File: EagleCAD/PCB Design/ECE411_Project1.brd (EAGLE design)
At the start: 160 x 100 mm, 29 parts, among them J1 0473460001_USBMICRO, SW1 FSM2JSMLTR, U1 ATS160SM-1, U2 MIC29310-5.0WU, U3 NCP5501DT50RKG

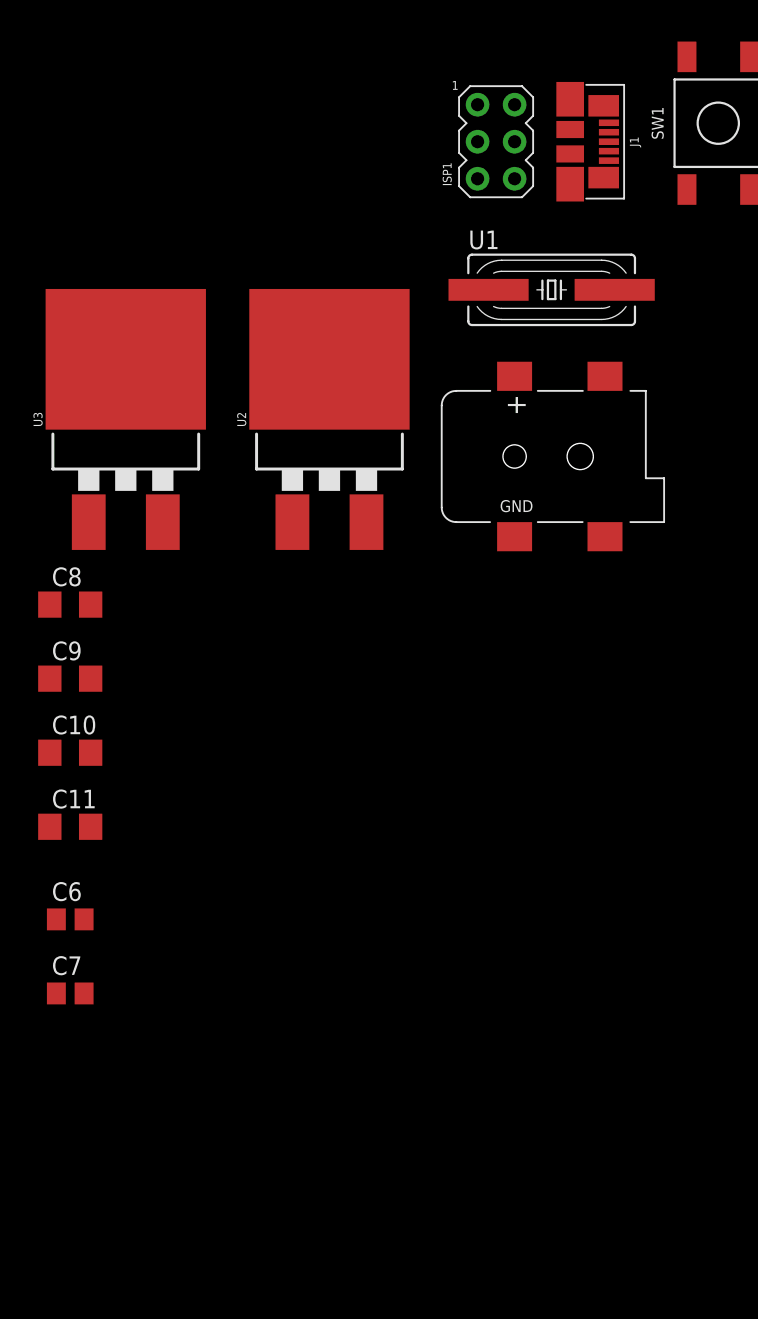
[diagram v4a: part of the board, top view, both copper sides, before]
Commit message: Updated schematic with new DC barrel component that is thru-hole 2.1MM size
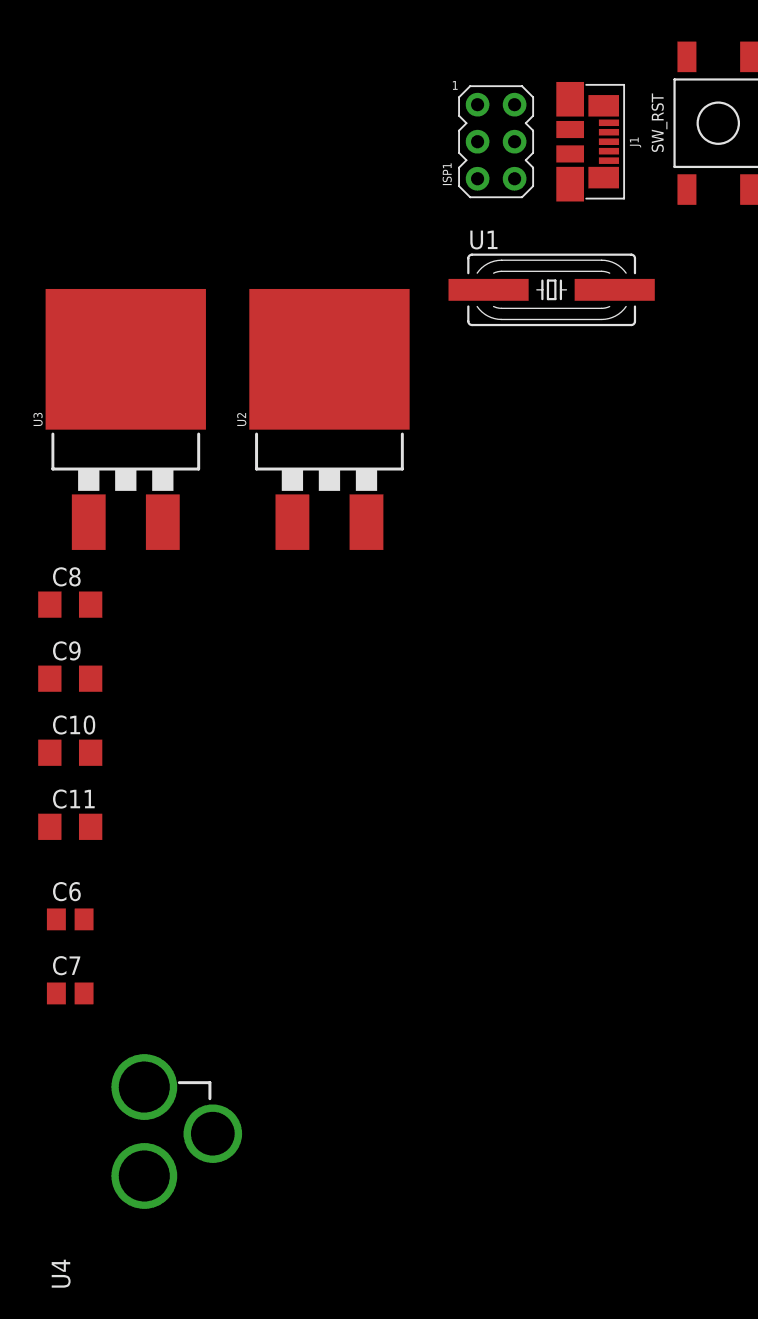
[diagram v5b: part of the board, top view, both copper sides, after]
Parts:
- removed CN1: (no value), adafruit:DCJACK_2MM_SMT
- added U4: DCJACK_2.1MM_PTH, DCBARREL_2.1MM:DCJACK_2.1MM_PTH
- renumbered SW1 to SW_RST
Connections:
- net N$1 renamed D+USB
- net N$2 renamed D+MCU
- net N$3 renamed D-USB
- net N$4 renamed D-MCU
- net GND: now also U4.GND, U4.GNDBREAK; no longer CN1.GND, CN1.GNDBREAK
- net N$22: now also U4.PWR; no longer CN1.PWR1
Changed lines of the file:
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@@
 <element name="LED2" library="led" library_urn="urn:adsk.eagle:library:259" package="1206" package3d_urn="urn:adsk.eagle:package:15796/1" value="" x="-67.31" y="-15.24"/>
 <element name="LED1" library="led" library_urn="urn:adsk.eagle:library:259" package="1206" package3d_urn="urn:adsk.eagle:package:15796/1" value="" x="-67.31" y="-20.32"/>
-<element name="SW1" library="Push_Button" package="FSM2JSMLTR" value="FSM2JSMLTR" x="-73.66" y="-49.53"/>
+<element name="SW_RST" library="Push_Button" package="FSM2JSMLTR" value="FSM2JSMLTR" x="-73.66" y="-49.53"/>
 <element name="J1" library="USB_Micro_and_AVRISP" package="MOLEX_USBMICRO" value="0473460001_USBMICRO" x="-83.82" y="-50.8"/>
 <element name="ISP1" library="USB_Micro_and_AVRISP" package="AVRISP" value="AVRISP-6" x="-88.9" y="-50.8"/>
 <element name="U1" library="Xtals" package="ATS160SM-1" value="ATS160SM-1" x="-85.09" y="-60.96"/>
-<element name="CN1" library="adafruit" library_urn="urn:adsk.eagle:library:420" package="DCJACK_2MM_SMT" package3d_urn="urn:adsk.eagle:package:6240730/1" value="" x="-87.63" y="-72.39"/>
 <element name="U2" library="Regulators" package="TO-263/D2PAK" value="MIC29310-5.0WU" x="-100.33" y="-69.85"/>
 <element name="U3" library="Regulators" package="TO-263/D2PAK" value="NCP5501DT50RKG" x="-114.3" y="-69.85"/>
@@
 <attribute name="SPICEPREFIX" value="C" x="-118.11" y="-109.22" size="1.778" layer="27" display="off"/>
 </element>
+<element name="U4" library="DCBARREL_2.1MM" package="DCJACK_2.1MM_PTH" value="DCJACK_2.1MM_PTH" x="-113.03" y="-129.54"/>
 </elements>
 <signals>
@@
 <contactref element="C4" pad="1"/>
 <contactref element="C3" pad="1"/>
-<contactref element="SW1" pad="4"/>
-<contactref element="SW1" pad="2"/>
+<contactref element="SW_RST" pad="4"/>
+<contactref element="SW_RST" pad="2"/>
 <contactref element="J1" pad="5"/>
 <contactref element="J1" pad="G6"/>
@@
 <contactref element="U2" pad="2"/>
 <contactref element="U3" pad="2"/>
-<contactref element="CN1" pad="GND"/>
-<contactref element="CN1" pad="GNDBREAK"/>
 <contactref element="C8" pad="2"/>
 <contactref element="C11" pad="2"/>
@@
 <contactref element="C6" pad="1"/>
 <contactref element="C7" pad="1"/>
+<contactref element="U4" pad="GND"/>
+<contactref element="U4" pad="GNDBREAK"/>
+<wire x1="-108.33" y1="-118.84" x2="-113.03" y2="-121.74" width="0" layer="19" extent="1-1"/>
+<wire x1="-119.06" y1="-109.22" x2="-113.03" y2="-121.74" width="0" layer="19" extent="1-1"/>
 <wire x1="-119.06" y1="-104.14" x2="-119.06" y2="-109.22" width="0" layer="19" extent="1-1"/>
 <wire x1="-116.71" y1="-97.79" x2="-119.06" y2="-104.14" width="0" layer="19" extent="1-1"/>
@@
 <wire x1="-114.3" y1="-65.725" x2="-116.71" y2="-82.55" width="0" layer="19" extent="1-1"/>
 <wire x1="-100.33" y1="-65.725" x2="-114.3" y2="-65.725" width="0" layer="19" extent="1-1"/>
-<wire x1="-87.63" y1="-77.89" x2="-100.33" y2="-65.725" width="0" layer="19" extent="1-1"/>
-<wire x1="-81.43" y1="-77.89" x2="-87.63" y2="-77.89" width="0" layer="19" extent="1-1"/>
 <wire x1="-87.63" y1="-53.34" x2="-100.33" y2="-65.725" width="0" layer="19" extent="1-1"/>
 <wire x1="-83.82" y1="-53.7125" x2="-87.63" y2="-53.34" width="0" layer="19" extent="1-1"/>
@@
 <wire x1="-15.24" y1="73.66" x2="-17.91" y2="68.58" width="0" layer="19" extent="1-1"/>
 </signal>
-<signal name="N$1">
+<signal name="D+USB">
 <contactref element="R1" pad="1"/>
 <contactref element="J1" pad="3"/>
 <wire x1="-28.092" y1="68.58" x2="-81.16" y2="-50.8" width="0" layer="19" extent="1-1"/>
 </signal>
-<signal name="N$2">
+<signal name="D+MCU">
 <contactref element="U$1" pad="4"/>
 <contactref element="R1" pad="2"/>
 <wire x1="-59.14" y1="35.89" x2="-25.248" y2="68.58" width="0" layer="19" extent="1-1"/>
 </signal>
-<signal name="N$3">
+<signal name="D-USB">
 <contactref element="R2" pad="1"/>
 <contactref element="J1" pad="2"/>
 <wire x1="-33.172" y1="68.58" x2="-81.16" y2="-50.15" width="0" layer="19" extent="1-1"/>
 </signal>
-<signal name="N$4">
+<signal name="D-MCU">
 <contactref element="U$1" pad="3"/>
 <contactref element="R2" pad="2"/>
@@
 <contactref element="U$1" pad="13"/>
 <contactref element="R5" pad="1"/>
-<contactref element="SW1" pad="3"/>
-<contactref element="SW1" pad="1"/>
+<contactref element="SW_RST" pad="3"/>
+<contactref element="SW_RST" pad="1"/>
 <contactref element="ISP1" pad="5"/>
 <wire x1="-75.81" y1="-44.98" x2="-90.17" y2="-53.34" width="0" layer="19" extent="1-1"/>
@@
 </signal>
 <signal name="N$22">
-<contactref element="CN1" pad="PWR1"/>
 <contactref element="U3" pad="1"/>
 <contactref element="U2" pad="1"/>
 <contactref element="C8" pad="1"/>
 <contactref element="C9" pad="1"/>
+<contactref element="U4" pad="PWR"/>
+<wire x1="-119.51" y1="-87.63" x2="-113.03" y2="-115.64" width="0" layer="19" extent="1-1"/>
 <wire x1="-119.51" y1="-82.55" x2="-119.51" y2="-87.63" width="0" layer="19" extent="1-1"/>
 <wire x1="-116.84" y1="-76.895" x2="-119.51" y2="-82.55" width="0" layer="19" extent="1-1"/>
 <wire x1="-102.87" y1="-76.895" x2="-116.84" y2="-76.895" width="0" layer="19" extent="1-1"/>
-<wire x1="-87.63" y1="-66.89" x2="-102.87" y2="-76.895" width="0" layer="19" extent="1-1"/>
 </signal>
 </signals>

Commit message: Started the PCB - Everything's on the board and messy!
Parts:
- moved U4 293.6 mm to (148.6, 3.81)
- moved C11 268.4 mm to (131.1, 1.79), turned to 180 degrees
- moved C10 257.7 mm to (121.4, 2.29)
- moved U2 243.5 mm to (128.3, 14.0)
- moved C9 242.6 mm to (107.4, 1.87)
- moved U3 233.5 mm to (104.1, 12.7)
- moved C8 228.5 mm to (94.0, 2.61), turned to 270 degrees
- moved SERVO1 218.6 mm to (153.7, 73.7), turned to 90 degrees
- moved BUTTON_PAD 208.4 mm to (153.7, 90.2), turned to 90 degrees
- moved C6 206.5 mm to (51.4, 13.9)
- moved C7 203.8 mm to (44.4, 13.8)
- moved SERVO2 171.8 mm to (153.7, 62.2), turned to 90 degrees
- moved J1 164.5 mm to (5.08, 87.6)
- moved U1 148.8 mm to (47.0, 7.62)
- moved ISP1 120.2 mm to (5.08, 24.1)
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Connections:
- net N$20 renamed XTAL2
- net N$21 renamed XTAL1
- net N$22 renamed UNREG_PWR
- net N$5 renamed UCAP
- removed net N$15: ISP1.2
- new net GNDBREAK: U4.GNDBREAK
- net GND: no longer U4.GNDBREAK
- net VCC: now also ISP1.2

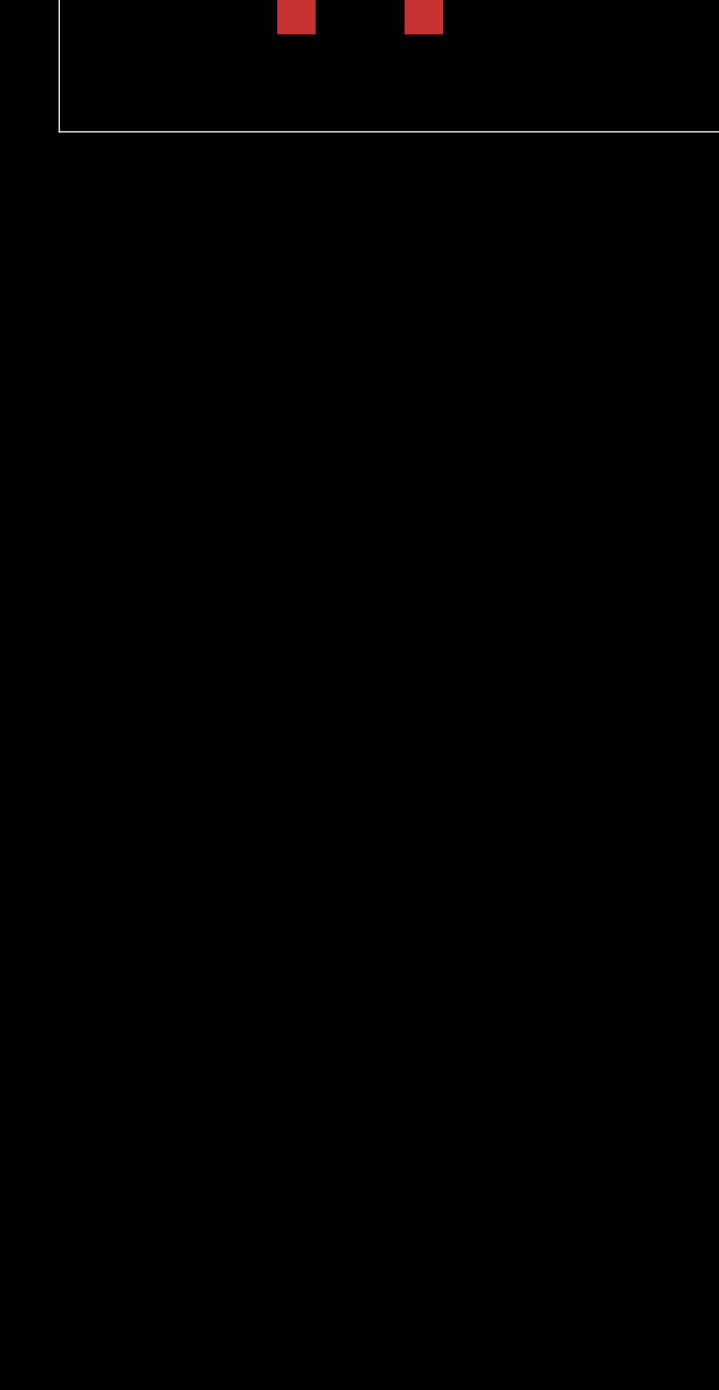
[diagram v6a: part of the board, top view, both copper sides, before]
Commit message: Added test points all over the place
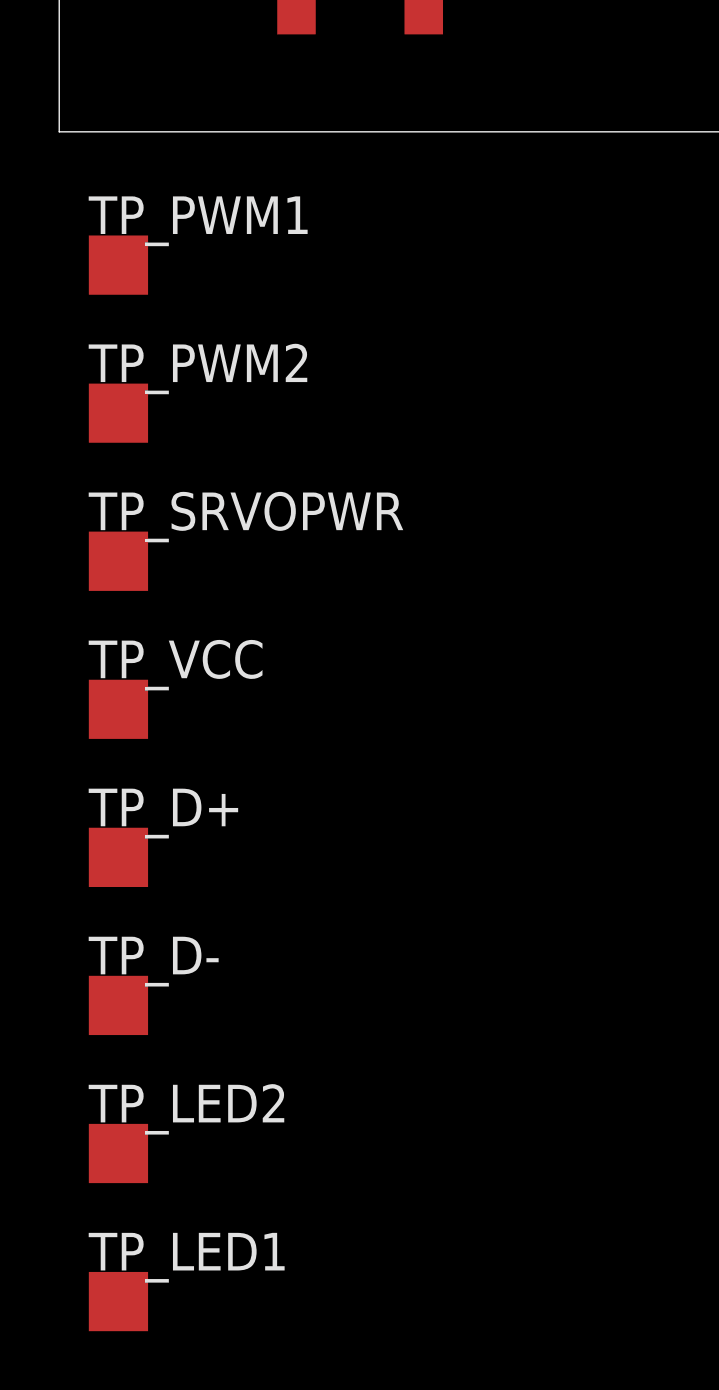
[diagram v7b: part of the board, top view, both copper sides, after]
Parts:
- added TP_D+, TP_D-, TP_LED1, TP_LED2, TP_PWM1, TP_PWM2, TP_SRVOPWR, TP_VCC: TPTP20SQ, BeagleBone_Blue_R3:TP20SQ
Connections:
- net D+MCU: now also TP_D+.TP
- net D-MCU: now also TP_D-.TP
- net N$6: now also TP_LED2.TP
- net N$8: now also TP_LED1.TP
- net PWM1: now also TP_PWM1.TP
- net PWM2: now also TP_PWM2.TP
- net SERVO_PWR: now also TP_SRVOPWR.TP
- net VCC: now also TP_VCC.TP
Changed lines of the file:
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@@
 </element>
 <element name="U4" library="DCBARREL_2.1MM" package="DCJACK_2.1MM_PTH" value="DCJACK_2.1MM_PTH" x="148.59" y="3.81"/>
+<element name="TP_PWM1" library="BeagleBone_Blue_R3" library_urn="urn:adsk.eagle:library:5828899" package="TP20SQ" package3d_urn="urn:adsk.eagle:package:5829471/1" value="TPTP20SQ" x="2" y="-4.5">
+<attribute name="TP_SIGNAL_NAME" value="" x="2" y="-4.5" size="1.778" layer="27" display="off"/>
+</element>
+<element name="TP_PWM2" library="BeagleBone_Blue_R3" library_urn="urn:adsk.eagle:library:5828899" package="TP20SQ" package3d_urn="urn:adsk.eagle:package:5829471/1" value="TPTP20SQ" x="2" y="-9.5">
+<attribute name="TP_SIGNAL_NAME" value="" x="2" y="-9.5" size="1.778" layer="27" display="off"/>
+</element>
+<element name="TP_SRVOPWR" library="BeagleBone_Blue_R3" library_urn="urn:adsk.eagle:library:5828899" package="TP20SQ" package3d_urn="urn:adsk.eagle:package:5829471/1" value="TPTP20SQ" x="2" y="-14.5">
+<attribute name="TP_SIGNAL_NAME" value="" x="2" y="-14.5" size="1.778" layer="27" display="off"/>
+</element>
+<element name="TP_VCC" library="BeagleBone_Blue_R3" library_urn="urn:adsk.eagle:library:5828899" package="TP20SQ" package3d_urn="urn:adsk.eagle:package:5829471/1" value="TPTP20SQ" x="2" y="-19.5">
+<attribute name="TP_SIGNAL_NAME" value="" x="2" y="-19.5" size="1.778" layer="27" display="off"/>
+</element>
+<element name="TP_D+" library="BeagleBone_Blue_R3" library_urn="urn:adsk.eagle:library:5828899" package="TP20SQ" package3d_urn="urn:adsk.eagle:package:5829471/1" value="TPTP20SQ" x="2" y="-24.5">
+<attribute name="TP_SIGNAL_NAME" value="" x="2" y="-24.5" size="1.778" layer="27" display="off"/>
+</element>
+<element name="TP_D-" library="BeagleBone_Blue_R3" library_urn="urn:adsk.eagle:library:5828899" package="TP20SQ" package3d_urn="urn:adsk.eagle:package:5829471/1" value="TPTP20SQ" x="2" y="-29.5">
+<attribute name="TP_SIGNAL_NAME" value="" x="2" y="-29.5" size="1.778" layer="27" display="off"/>
+</element>
+<element name="TP_LED2" library="BeagleBone_Blue_R3" library_urn="urn:adsk.eagle:library:5828899" package="TP20SQ" package3d_urn="urn:adsk.eagle:package:5829471/1" value="TPTP20SQ" x="2" y="-34.5">
+<attribute name="TP_SIGNAL_NAME" value="" x="2" y="-34.5" size="1.778" layer="27" display="off"/>
+</element>
+<element name="TP_LED1" library="BeagleBone_Blue_R3" library_urn="urn:adsk.eagle:library:5828899" package="TP20SQ" package3d_urn="urn:adsk.eagle:package:5829471/1" value="TPTP20SQ" x="2" y="-39.5">
+<attribute name="TP_SIGNAL_NAME" value="" x="2" y="-39.5" size="1.778" layer="27" display="off"/>
+</element>
 </elements>
 <signals>
@@
 <contactref element="U$1" pad="4"/>
 <contactref element="R1" pad="2"/>
+<contactref element="TP_D+" pad="TP"/>
 <wire x1="14.52" y1="25.73" x2="40.252" y2="73.58" width="0" layer="19" extent="1-1"/>
+<wire x1="2" y1="-24.5" x2="14.52" y2="25.73" width="0" layer="19" extent="1-1"/>
 </signal>
 <signal name="D-USB">
@@
 <contactref element="U$1" pad="3"/>
 <contactref element="R2" pad="2"/>
+<contactref element="TP_D-" pad="TP"/>
 <wire x1="14.52" y1="26.53" x2="35.172" y2="73.58" width="0" layer="19" extent="1-1"/>
+<wire x1="2" y1="-29.5" x2="14.52" y2="26.53" width="0" layer="19" extent="1-1"/>
 </signal>
 <signal name="UCAP">
@@
 <contactref element="U$1" pad="18"/>
 <contactref element="R3" pad="2"/>
+<contactref element="TP_LED2" pad="TP"/>
 <wire x1="21.12" y1="18.33" x2="12.112" y2="55.69" width="0" layer="19" extent="1-1"/>
+<wire x1="2" y1="-34.5" x2="21.12" y2="18.33" width="0" layer="19" extent="1-1"/>
 </signal>
 <signal name="N$9">
@@
 <contactref element="C10" pad="1"/>
 <contactref element="ISP1" pad="2"/>
+<contactref element="TP_VCC" pad="TP"/>
 <wire x1="106.68" y1="5.655" x2="119.99" y2="2.29" width="0" layer="19" extent="1-1"/>
-<wire x1="6.35" y1="26.67" x2="106.68" y2="5.655" width="0" layer="19" extent="1-1"/>
-<wire x1="17.92" y1="18.33" x2="6.35" y2="26.67" width="0" layer="19" extent="1-1"/>
-<wire x1="26.12" y1="20.93" x2="17.92" y2="18.33" width="0" layer="19" extent="1-1"/>
-<wire x1="24.32" y1="29.93" x2="26.12" y2="20.93" width="0" layer="19" extent="1-1"/>
+<wire x1="40.39" y1="39.58" x2="106.68" y2="5.655" width="0" layer="19" extent="1-1"/>
+<wire x1="34.79" y1="39.53" x2="40.39" y2="39.58" width="0" layer="19" extent="1-1"/>
+<wire x1="28.44" y1="39.53" x2="34.79" y2="39.53" width="0" layer="19" extent="1-1"/>
+<wire x1="22.09" y1="39.53" x2="28.44" y2="39.53" width="0" layer="19" extent="1-1"/>
+<wire x1="24.32" y1="29.93" x2="22.09" y2="39.53" width="0" layer="19" extent="1-1"/>
 <wire x1="16.32" y1="29.93" x2="24.32" y2="29.93" width="0" layer="19" extent="1-1"/>
-<wire x1="28.44" y1="39.53" x2="16.32" y2="29.93" width="0" layer="19" extent="1-1"/>
-<wire x1="22.09" y1="39.53" x2="28.44" y2="39.53" width="0" layer="19" extent="1-1"/>
-<wire x1="34.79" y1="39.53" x2="28.44" y2="39.53" width="0" layer="19" extent="1-1"/>
-<wire x1="30.092" y1="73.58" x2="34.79" y2="39.53" width="0" layer="19" extent="1-1"/>
-<wire x1="40.39" y1="39.58" x2="30.092" y2="73.58" width="0" layer="19" extent="1-1"/>
+<wire x1="26.12" y1="20.93" x2="24.32" y2="29.93" width="0" layer="19" extent="1-1"/>
+<wire x1="17.92" y1="18.33" x2="26.12" y2="20.93" width="0" layer="19" extent="1-1"/>
+<wire x1="6.35" y1="26.67" x2="16.32" y2="29.93" width="0" layer="19" extent="1-1"/>
+<wire x1="30.092" y1="73.58" x2="28.44" y2="39.53" width="0" layer="19" extent="1-1"/>
+<wire x1="2" y1="-19.5" x2="17.92" y2="18.33" width="0" layer="19" extent="1-1"/>
 </signal>
 <signal name="PWM2">
 <contactref element="U$1" pad="29"/>
 <contactref element="SERVO2" pad="1"/>
+<contactref element="TP_PWM2" pad="TP"/>
 <wire x1="26.12" y1="24.93" x2="153.67" y2="59.69" width="0" layer="19" extent="1-1"/>
+<wire x1="2" y1="-9.5" x2="26.12" y2="24.93" width="0" layer="19" extent="1-1"/>
 </signal>
 <signal name="PWM1">
 <contactref element="U$1" pad="30"/>
 <contactref element="SERVO1" pad="1"/>
-<wire x1="153.67" y1="71.12" x2="26.12" y2="25.73" width="0" layer="19" extent="1-1"/>
+<contactref element="TP_PWM1" pad="TP"/>
+<wire x1="26.12" y1="25.73" x2="153.67" y2="71.12" width="0" layer="19" extent="1-1"/>
+<wire x1="2" y1="-4.5" x2="26.12" y2="25.73" width="0" layer="19" extent="1-1"/>
 </signal>
 <signal name="N$8">
 <contactref element="U$1" pad="19"/>
 <contactref element="R4" pad="2"/>
+<contactref element="TP_LED1" pad="TP"/>
 <wire x1="21.92" y1="18.33" x2="12.112" y2="50.61" width="0" layer="19" extent="1-1"/>
+<wire x1="2" y1="-39.5" x2="21.92" y2="18.33" width="0" layer="19" extent="1-1"/>
 </signal>
 <signal name="N$7">
@@
 <contactref element="U2" pad="3"/>
 <contactref element="C11" pad="1"/>
-<wire x1="130.81" y1="6.925" x2="132.51" y2="1.79" width="0" layer="19" extent="1-1"/>
-<wire x1="153.67" y1="73.66" x2="130.81" y2="6.925" width="0" layer="19" extent="1-1"/>
+<contactref element="TP_SRVOPWR" pad="TP"/>
 <wire x1="153.67" y1="62.23" x2="153.67" y2="73.66" width="0" layer="19" extent="1-1"/>
+<wire x1="130.81" y1="6.925" x2="153.67" y2="62.23" width="0" layer="19" extent="1-1"/>
+<wire x1="132.51" y1="1.79" x2="130.81" y2="6.925" width="0" layer="19" extent="1-1"/>
+<wire x1="2" y1="-14.5" x2="130.81" y2="6.925" width="0" layer="19" extent="1-1"/>
 </signal>
 <signal name="XTAL2">
